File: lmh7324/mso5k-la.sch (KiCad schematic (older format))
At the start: 2 parts, among them J1 output, J2 input

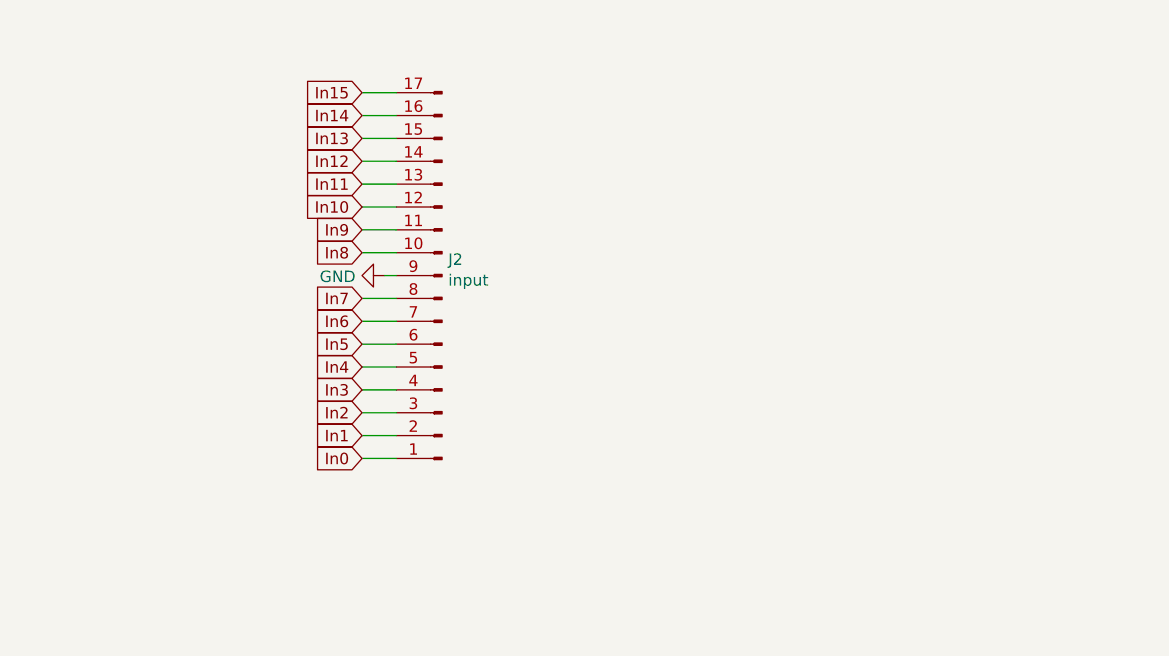
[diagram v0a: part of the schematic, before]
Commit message: Trying mass-edit of net names
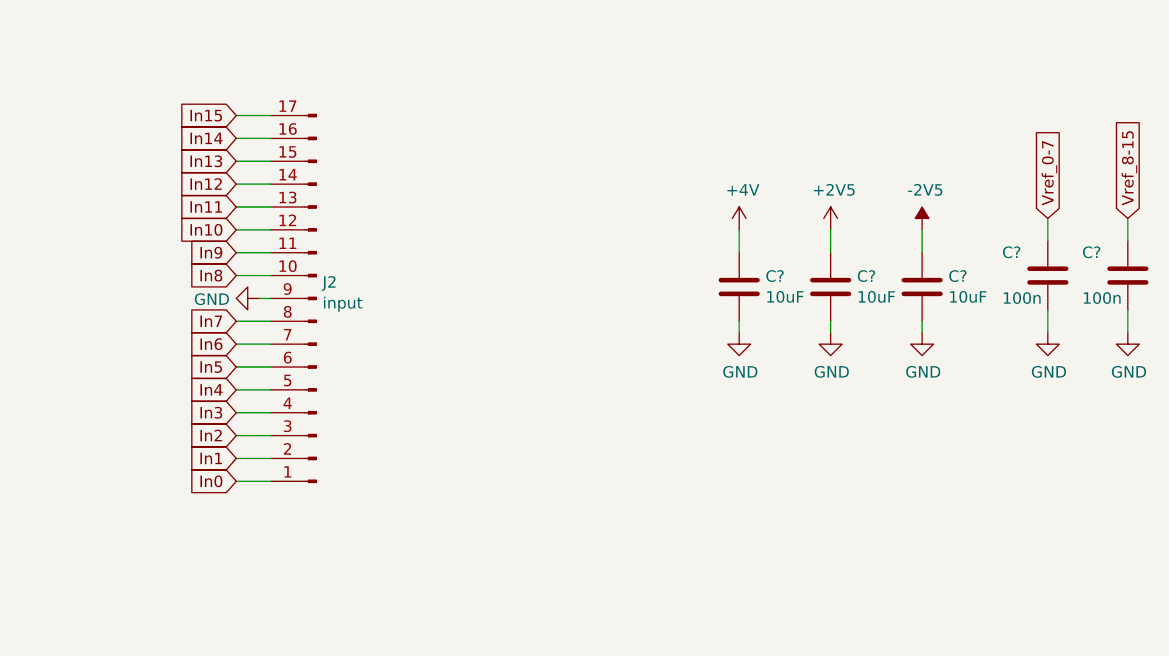
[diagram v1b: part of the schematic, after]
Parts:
- added C? (x2): 100n, symbol Device:C
- added C? (x3): 10uF, symbol Device:C
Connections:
- net +2V5: now also C?.1
- net +4V: now also C?.1
- net -2V5: now also C?.1
- net GND: now also C?.2, C?.2, C?.2, C?.2, C?.2
- net Vref_0-7: now also C?.1
- net Vref_8-15: now also C?.1
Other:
- moved on the sheet: J2

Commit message: completed core layout of 16 channel lmh7324 design
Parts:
- C101, C102, C103: renamed from C?; footprint (none) -> Capacitors_SMD.pretty:C_1206
- C104, C105: renamed from C?; footprint (none) -> Capacitors_SMD.pretty:C_0603
- J101: renamed from J1; footprint (none) -> Connectors_IDC.pretty:IDC-Header_2x25_Pitch2.54mm_Angled
- J102: renamed from J2; footprint (none) -> Connector_PinHeader_2.54mm:PinHeader_1x17_P2.54mm_Horizontal
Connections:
- net D0 renamed D0+
- net D1 renamed D1+
- net D10 renamed D10+
- net D11 renamed D11+
- net D12 renamed D12+
- net D13 renamed D13+
- net D14 renamed D14+
- net D15 renamed D15+
- net D2 renamed D2+
- net D3 renamed D3+
- net D4 renamed D4+
- net D5 renamed D5+
- net D6 renamed D6+
- net D7 renamed D7+
- net D8 renamed D8+
- net D9 renamed D9+
- net ~D0 renamed D0-
- net ~D1 renamed D1-
- net ~D10 renamed D10-
- net ~D11 renamed D11-
- net ~D12 renamed D12-
- net ~D13 renamed D13-
- net ~D14 renamed D14-
- net ~D15 renamed D15-
- net ~D2 renamed D2-
- net ~D3 renamed D3-
- net ~D4 renamed D4-
- net ~D5 renamed D5-
- net ~D6 renamed D6-
- net ~D7 renamed D7-
- net ~D8 renamed D8-
- net ~D9 renamed D9-
